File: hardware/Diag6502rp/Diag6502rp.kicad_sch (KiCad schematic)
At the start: 4 parts, among them J1 Conn_01x21_Pin, J2 Conn_01x21_Socket, J3 Conn_01x21_Pin, J4 Conn_01x21_Socket

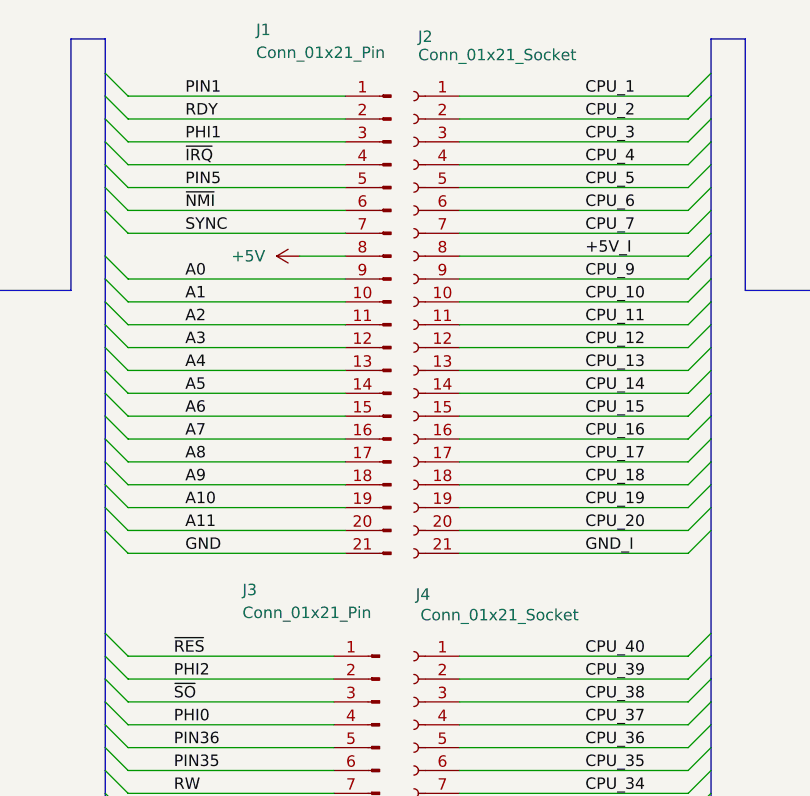
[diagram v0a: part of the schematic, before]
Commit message: Changed TSX0108e foorprint to TSSOP20 for easier routing.
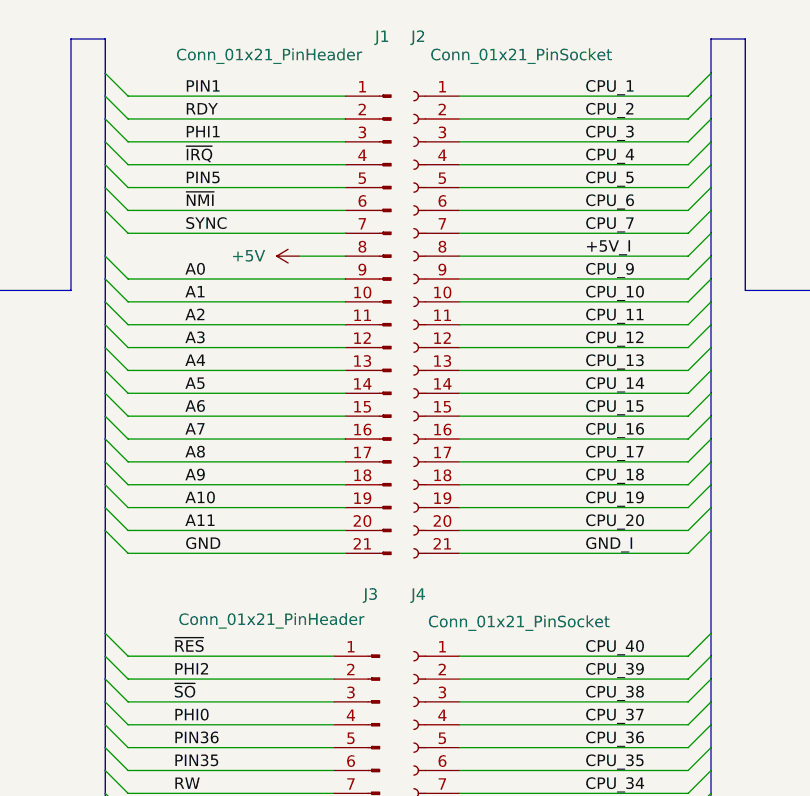
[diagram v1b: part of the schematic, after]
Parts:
- J1, J3: value Conn_01x21_Pin -> Conn_01x21_PinHeader; footprint Connector_PinSocket_2.54mm:PinSocket_1x21_P2.54mm_Vertical -> Connector_PinHeader_2.54mm:PinHeader_1x21_P2.54mm_Vertical
- J2, J4: value Conn_01x21_Socket -> Conn_01x21_PinSocket; footprint Connector_PinHeader_2.54mm:PinHeader_1x21_P2.54mm_Vertical -> Connector_PinSocket_2.54mm:PinSocket_1x21_P2.54mm_Vertical
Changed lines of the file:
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@@
 		(dnp no)
 		(property "Reference" "J1"
-			(at 176.784 23.114 0)
+			(at 189.992 23.876 0)
 			(effects
 				(font
@@
 			)
 		)
-		(property "Value" "Conn_01x21_Pin"
-			(at 176.784 25.654 0)
+		(property "Value" "Conn_01x21_PinHeader"
+			(at 167.894 25.908 0)
 			(effects
 				(font
@@
 			)
 		)
-		(property "Footprint" "Connector_PinSocket_2.54mm:PinSocket_1x21_P2.54mm_Vertical"
+		(property "Footprint" "Connector_PinHeader_2.54mm:PinHeader_1x21_P2.54mm_Vertical"
 			(at 191.77 55.88 0)
 			(effects
@@
 		(dnp no)
 		(property "Reference" "J2"
-			(at 195.58 23.876 0)
-			(effects
-				(font
-					(size 1.27 1.27)
-				)
-			)
-		)
-		(property "Value" "Conn_01x21_Socket"
-			(at 203.581 25.908 0)
-			(effects
-				(font
-					(size 1.27 1.27)
-				)
-			)
-		)
-		(property "Footprint" "Connector_PinHeader_2.54mm:PinHeader_1x21_P2.54mm_Vertical"
+			(at 194.818 23.876 0)
+			(effects
+				(font
+					(size 1.27 1.27)
+				)
+			)
+		)
+		(property "Value" "Conn_01x21_PinSocket"
+			(at 206.248 25.908 0)
+			(effects
+				(font
+					(size 1.27 1.27)
+				)
+			)
+		)
+		(property "Footprint" "Connector_PinSocket_2.54mm:PinSocket_1x21_P2.54mm_Vertical"
 			(at 194.31 55.88 0)
 			(effects
@@
 		(dnp no)
 		(property "Reference" "J3"
-			(at 175.26 85.344 0)
+			(at 188.722 85.852 0)
 			(effects
 				(font
@@
 			)
 		)
-		(property "Value" "Conn_01x21_Pin"
-			(at 175.26 87.884 0)
+		(property "Value" "Conn_01x21_PinHeader"
+			(at 168.148 88.646 0)
 			(effects
 				(font
@@
 			)
 		)
-		(property "Footprint" "Connector_PinSocket_2.54mm:PinSocket_1x21_P2.54mm_Vertical"
+		(property "Footprint" "Connector_PinHeader_2.54mm:PinHeader_1x21_P2.54mm_Vertical"
 			(at 190.5 118.11 0)
 			(effects
@@
 		(dnp no)
 		(property "Reference" "J4"
-			(at 195.326 85.852 0)
-			(effects
-				(font
-					(size 1.27 1.27)
-				)
-			)
-		)
-		(property "Value" "Conn_01x21_Socket"
-			(at 203.835 88.138 0)
-			(effects
-				(font
-					(size 1.27 1.27)
-				)
-			)
-		)
-		(property "Footprint" "Connector_PinHeader_2.54mm:PinHeader_1x21_P2.54mm_Vertical"
+			(at 194.818 85.852 0)
+			(effects
+				(font
+					(size 1.27 1.27)
+				)
+			)
+		)
+		(property "Value" "Conn_01x21_PinSocket"
+			(at 205.994 88.9 0)
+			(effects
+				(font
+					(size 1.27 1.27)
+				)
+			)
+		)
+		(property "Footprint" "Connector_PinSocket_2.54mm:PinSocket_1x21_P2.54mm_Vertical"
 			(at 194.31 118.11 0)
 			(effects

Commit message: Main design completed
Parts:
- added J8: Conn_01x02_Socket, Connector_PinSocket_2.54mm:PinSocket_1x02_P2.54mm_Vertical, symbol Connector:Conn_01x02_Socket
- added J9: Conn_01x02_Pin, Connector_PinHeader_2.54mm:PinHeader_1x02_P2.54mm_Vertical, symbol Connector:Conn_01x02_Pin
- J1, J3: value Conn_01x21_PinHeader -> Conn_01x20_PinHeader; footprint Connector_PinHeader_2.54mm:PinHeader_1x21_P2.54mm_Vertical -> Connector_PinHeader_2.54mm:PinHeader_1x20_P2.54mm_Vertical; symbol Connector:Conn_01x21_Pin -> Connector:Conn_01x20_Pin
- J2: footprint Connector_PinSocket_2.54mm:PinSocket_1x21_P2.54mm_Vertical -> Connector_PinSocket_2.54mm:PinSocket_1x20_P2.54mm_Vertical; symbol Connector:Conn_01x21_Socket -> Connector:Conn_01x20_Socket
- J4: value Conn_01x21_PinSocket -> Conn_01x20_PinSocket; footprint Connector_PinSocket_2.54mm:PinSocket_1x21_P2.54mm_Vertical -> Connector_PinSocket_2.54mm:PinSocket_1x20_P2.54mm_Vertical; symbol Connector:Conn_01x21_Socket -> Connector:Conn_01x20_Socket
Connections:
- net +3V3: now also J9.2 (Pin_2); no longer J3.21 (Pin_21)
- net +3V3_I: now also J8.2 (Pin_2); no longer J4.21 (Pin_21)
- net GND: now also J9.1 (Pin_1); no longer J1.21 (Pin_21)
- net GND_I: now also J8.1 (Pin_1); no longer J2.21 (Pin_21)

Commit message: Cleanup, Fiduciaries, component spacing
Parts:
- J1, J3: LCSC Part # (none) -> C50981
- J2: value Conn_01x21_PinSocket -> Conn_01x20_PinSocket; LCSC Part # (none) -> C7499336
- J4: LCSC Part # (none) -> C7499336
- J8: value Conn_01x02_Socket -> Conn_01x02_PinSocket; LCSC Part # (none) -> C7499322
- J9: value Conn_01x02_Pin -> Conn_01x02_PinHeader; LCSC Part # (none) -> C492401
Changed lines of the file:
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@@
+			)
+		)
+		(property "LCSC Part #" "C50981"
+			(at 191.77 53.34 0)
+			(effects
+				(font
+					(size 1.27 1.27)
+				)
+				(hide yes)
+			)
+		)
+		(property "Mouser Part #" ""
+			(at 191.77 53.34 0)
+			(effects
+				(font
+					(size 1.27 1.27)
+				)
+				(hide yes)
+			)
+		)
+		(property "LCSC Name" ""
+			(at 191.77 53.34 0)
+			(effects
+				(font
+					(size 1.27 1.27)
+				)
+				(hide yes)
 			)
 		)
@@
 			)
 		)
-		(property "Value" "Conn_01x02_Pin"
+		(property "Value" "Conn_01x02_PinHeader"
 			(at 189.992 145.542 0)
 			(effects
@@
 		)
 		(property "Description" "Generic connector, single row, 01x02, script generated"
+			(at 190.5 153.67 0)
+			(effects
+				(font
+					(size 1.27 1.27)
+				)
+				(hide yes)
+			)
+		)
+		(property "LCSC Part #" "C492401"
+			(at 190.5 153.67 0)
+			(effects
+				(font
+					(size 1.27 1.27)
+				)
+				(hide yes)
+			)
+		)
+		(property "Mouser Part #" ""
+			(at 190.5 153.67 0)
+			(effects
+				(font
+					(size 1.27 1.27)
+				)
+				(hide yes)
+			)
+		)
+		(property "LCSC Name" ""
 			(at 190.5 153.67 0)
 			(effects
@@
 			)
 		)
-		(property "Value" "Conn_01x21_PinSocket"
+		(property "Value" "Conn_01x20_PinSocket"
 			(at 206.248 25.908 0)
 			(effects
@@
 		)
 		(property "Description" "Generic connector, single row, 01x20, script generated"
+			(at 194.31 53.34 0)
+			(effects
+				(font
+					(size 1.27 1.27)
+				)
+				(hide yes)
+			)
+		)
+		(property "LCSC Part #" "C7499336"
+			(at 194.31 53.34 0)
+			(effects
+				(font
+					(size 1.27 1.27)
+				)
+				(hide yes)
+			)
+		)
+		(property "Mouser Part #" ""
+			(at 194.31 53.34 0)
+			(effects
+				(font
+					(size 1.27 1.27)
+				)
+				(hide yes)
+			)
+		)
+		(property "LCSC Name" ""
 			(at 194.31 53.34 0)
 			(effects
@@
 			)
 		)
-		(property "Value" "Conn_01x02_Socket"
+		(property "Value" "Conn_01x02_PinSocket"
 			(at 194.31 145.542 0)
 			(effects
@@
 		)
 		(property "Description" "Generic connector, single row, 01x02, script generated"
+			(at 194.31 153.67 0)
+			(effects
+				(font
+					(size 1.27 1.27)
+				)
+				(hide yes)
+			)
+		)
+		(property "LCSC Part #" "C7499322"
+			(at 194.31 153.67 0)
+			(effects
+				(font
+					(size 1.27 1.27)
+				)
+				(hide yes)
+			)
+		)
+		(property "Mouser Part #" ""
+			(at 194.31 153.67 0)
+			(effects
+				(font
+					(size 1.27 1.27)
+				)
+				(hide yes)
+			)
+		)
+		(property "LCSC Name" ""
 			(at 194.31 153.67 0)
 			(effects
@@
 			)
 		)
+		(property "LCSC Part #" "C50981"
+			(at 190.5 115.57 0)
+			(effects
+				(font
+					(size 1.27 1.27)
+				)
+				(hide yes)
+			)
+		)
+		(property "Mouser Part #" ""
+			(at 190.5 115.57 0)
+			(effects
+				(font
+					(size 1.27 1.27)
+				)
+				(hide yes)
+			)
+		)
+		(property "LCSC Name" ""
+			(at 190.5 115.57 0)
+			(effects
+				(font
+					(size 1.27 1.27)
+				)
+				(hide yes)
+			)
+		)
 		(pin "14"
 		)
@@
 			(at 194.31 115.57 0)
 			(effects
+				(font
+					(size 1.27 1.27)
+				)
+				(hide yes)
+			)
+		)
+		(property "LCSC Part #" "C7499336"
+			(at 194.31 115.57 0)
+			(effects
+				(font
+					(size 1.27 1.27)
+				)
+				(hide yes)
+			)
+		)
+		(property "Mouser Part #" ""
+			(at 194.31 115.57 0)
+			(effects
+				(font
+					(size 1.27 1.27)
+				)
+				(hide yes)
+			)
+		)
+		(property "LCSC Name" ""
+			(at 194.31 115.57 0)
+			(effects
